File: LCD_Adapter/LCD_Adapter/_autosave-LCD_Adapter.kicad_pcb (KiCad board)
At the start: 4 copper layers, 47 x 75 mm, 56 parts, among them J1 Conn_01x10, J2 FH12-30S-0.5SH_55_, J4 1-1734248-5, J5 FH12-30S-0.5SH_55_, J6 2-1734248-0, U1 TLV75801PDBV, U2 TLV75801PDBV, U3 TPS61042DRBR

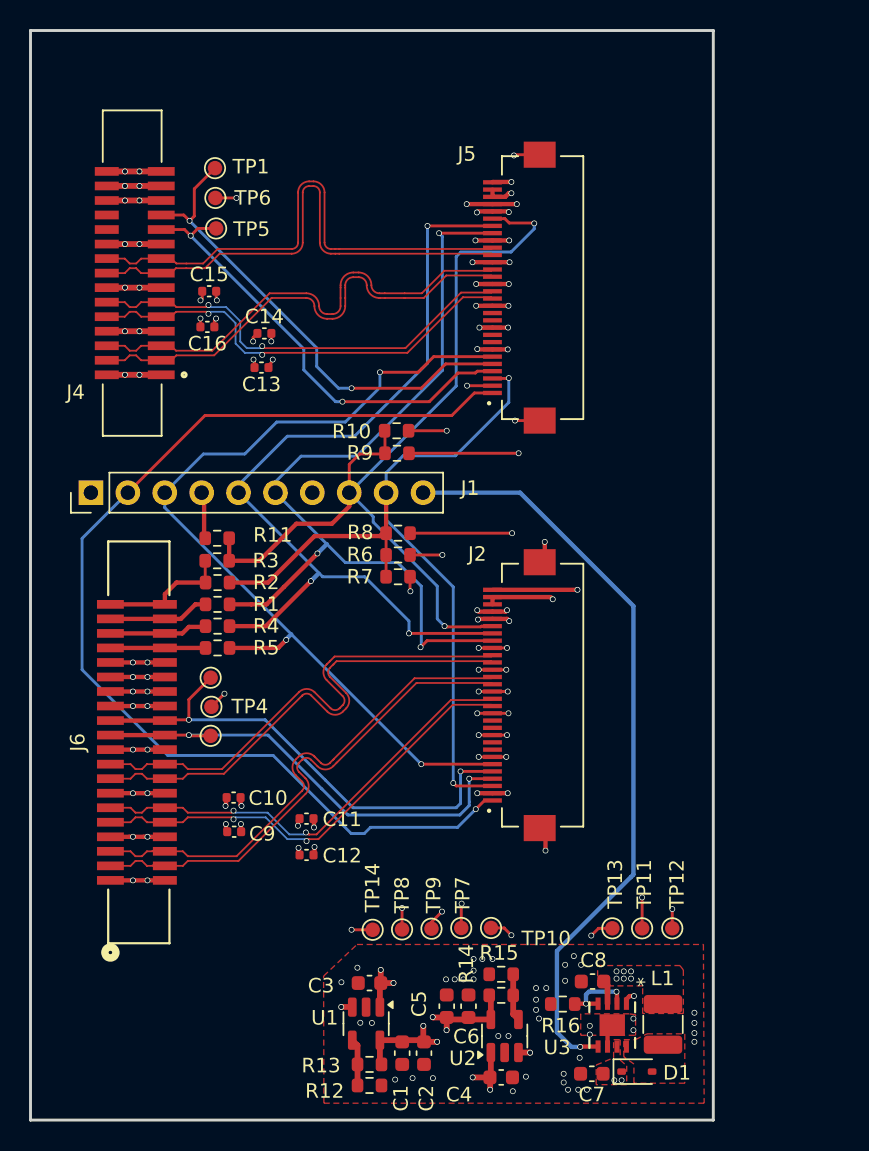
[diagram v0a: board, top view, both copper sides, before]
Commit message: adapter board done. ordered
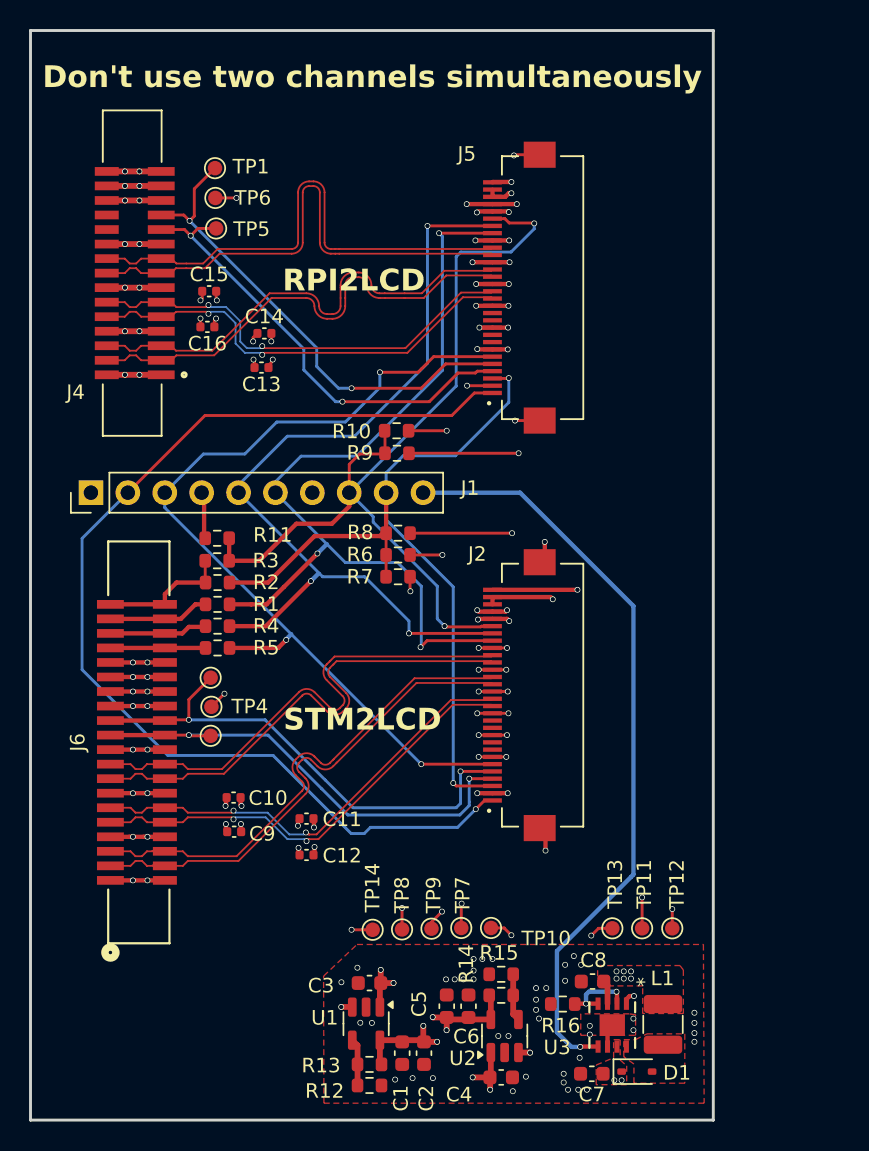
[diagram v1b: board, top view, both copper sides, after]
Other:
- board text added: "Don't use two channels simultaneously"
- board text added: "RPI2LCD"
- board text added: "STM2LCD"
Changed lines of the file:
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@@
 		(layer "Edge.Cuts")
+	)
+	(gr_text "STM2LCD\n"
+		(at 113.15 67.8 0)
+		(layer "F.SilkS")
+		(effects
+			(font
+				(size 1.5 1.5)
+				(thickness 0.3)
+				(bold yes)
+			)
+			(justify left bottom)
+		)
+	)
+	(gr_text "Don't use two channels simultaneously"
+		(at 96.575 23.575 0)
+		(layer "F.SilkS")
+		(effects
+			(font
+				(size 1.5 1.5)
+				(thickness 0.3)
+				(bold yes)
+			)
+			(justify left bottom)
+		)
+	)
+	(gr_text "RPI2LCD\n"
+		(at 113.1 37.575 0)
+		(layer "F.SilkS")
+		(effects
+			(font
+				(size 1.5 1.5)
+				(thickness 0.3)
+				(bold yes)
+			)
+			(justify left bottom)
+		)
 	)
 	(segment
